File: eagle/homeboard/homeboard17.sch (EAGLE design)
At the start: 127 parts, among them IC1 XCF02S, IC2 25LC080SN, IC3 ATMEGA32U2-TQFP, Q5 BC848SMD, Q6 BC848SMD, Q7 BC848SMD, Q8 BC848SMD, T1 BSS138, T2 BC848, T3 BSS138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

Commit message: cas
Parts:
- removed X1: 1503_04, con-lumberg:1503_04
- added T4: BC848, transistor:BC848
- added X8: STEREOJACK, cpcfpga:STEREOJACK
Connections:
- removed net AASA: SV1.8, U1B5.IO_L31N_5D4
- removed net N$104: SV1.6, U1B5.IO_L28N_5D6
- removed net QQQQ: SV1.7, U1B5.IO_L31P_5D5
- new net AA: SV1.6, U1B5.IO_L28P_5D7
- new net ABAB: SV1.8, U1B5.IO_L31P_5D5
- new net BB: SV1.7, U1B5.IO_L28N_5D6
- net CASIN: now also U1B2.IO_L01P_2VRN_2
- net CSYNC: now also U1B5.IO_L31N_5D4; no longer U1B5.IO_L28P_5D7
- net GND: now also X8.1; no longer X1.2
- net N$61: now also X8.2, X8.3, X8.4, X8.5; no longer X1.1
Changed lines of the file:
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@@
 <part name="C2" library="resistor" deviceset="C-EU" device="C0603" value="100nF"/>
 <part name="T2" library="transistor" deviceset="BC848" device=""/>
-<part name="X1" library="con-lumberg" deviceset="1503_04" device=""/>
 <part name="R22" library="rcl" deviceset="R-EU_" device="R0805" value="1000"/>
 <part name="X3" library="mini_din" deviceset="MINI_DIN_6" device=""/>
@@
 <part name="PWR_HDR" library="jumper" deviceset="JP1Q" device=""/>
 <part name="SUPPLY21" library="supply2" deviceset="GND" device=""/>
+<part name="X8" library="cpcfpga" deviceset="STEREOJACK" device=""/>
+<part name="T4" library="transistor" deviceset="BC848" device=""/>
 </parts>
 <sheets>
@@
 <instance part="C2" gate="G$1" x="492.76" y="-50.8" rot="R90"/>
 <instance part="T2" gate="G$1" x="513.08" y="-50.8"/>
-<instance part="X1" gate="G$1" x="464.82" y="-55.88" rot="R180"/>
 <instance part="R22" gate="G$1" x="508" y="-35.56" rot="R180"/>
 <instance part="X3" gate="G$1" x="279.4" y="-226.06"/>
@@
 <instance part="PWR_HDR" gate="A" x="-297.18" y="50.8" rot="R90"/>
 <instance part="SUPPLY21" gate="GND" x="-289.56" y="38.1"/>
+<instance part="X8" gate="1" x="447.04" y="-58.42" rot="MR0"/>
+<instance part="T4" gate="G$1" x="416.56" y="-33.02"/>
 </instances>
 <busses>
@@
 <wire x1="500.38" y1="-66.04" x2="515.62" y2="-66.04" width="0.1524" layer="91"/>
 <pinref part="R17" gate="G$1" pin="1"/>
-<wire x1="469.9" y1="-66.04" x2="487.68" y2="-66.04" width="0.1524" layer="91"/>
+<wire x1="459.74" y1="-66.04" x2="487.68" y2="-66.04" width="0.1524" layer="91"/>
 <wire x1="487.68" y1="-66.04" x2="500.38" y2="-66.04" width="0.1524" layer="91"/>
 <junction x="487.68" y="-66.04"/>
 <junction x="500.38" y="-66.04"/>
-<pinref part="X1" gate="G$1" pin="2"/>
-<wire x1="469.9" y1="-66.04" x2="469.9" y2="-58.42" width="0.1524" layer="91"/>
 <wire x1="523.24" y1="-66.04" x2="515.62" y2="-66.04" width="0.1524" layer="91"/>
 <junction x="515.62" y="-66.04"/>
 <label x="523.24" y="-66.04" size="1.778" layer="95"/>
+<pinref part="X8" gate="1" pin="1"/>
 </segment>
 <segment>
@@
 </segment>
 <segment>
-<wire x1="99.06" y1="-66.04" x2="139.7" y2="-66.04" width="0.1524" layer="91"/>
-<wire x1="139.7" y1="-66.04" x2="139.7" y2="-40.64" width="0.1524" layer="91"/>
-<pinref part="U1" gate="B5" pin="IO_L28P_5D7"/>
-<label x="99.06" y="-66.04" size="1.778" layer="95"/>
+<pinref part="U1" gate="B5" pin="IO_L31N_5D4"/>
+<wire x1="99.06" y1="-73.66" x2="137.16" y2="-73.66" width="0.1524" layer="91"/>
+<wire x1="137.16" y1="-73.66" x2="137.16" y2="-40.64" width="0.1524" layer="91"/>
+<label x="99.06" y="-73.66" size="1.778" layer="95"/>
 </segment>
 </net>
@@
 <junction x="515.62" y="-55.88"/>
 <label x="523.24" y="-55.88" size="1.778" layer="95"/>
+</segment>
+<segment>
+<pinref part="U1" gate="B2" pin="IO_L01P_2VRN_2"/>
+<wire x1="210.82" y1="55.88" x2="231.14" y2="55.88" width="0.1524" layer="91"/>
+<label x="231.14" y="55.88" size="1.778" layer="95"/>
 </segment>
 </net>
@@
 <wire x1="490.22" y1="-50.8" x2="487.68" y2="-50.8" width="0.1524" layer="91"/>
 <pinref part="R17" gate="G$1" pin="2"/>
-<wire x1="487.68" y1="-50.8" x2="469.9" y2="-50.8" width="0.1524" layer="91"/>
 <wire x1="487.68" y1="-55.88" x2="487.68" y2="-50.8" width="0.1524" layer="91"/>
+<pinref part="X8" gate="1" pin="2"/>
+<wire x1="459.74" y1="-63.5" x2="464.82" y2="-63.5" width="0.1524" layer="91"/>
+<wire x1="464.82" y1="-63.5" x2="477.52" y2="-63.5" width="0.1524" layer="91"/>
+<wire x1="477.52" y1="-63.5" x2="477.52" y2="-55.88" width="0.1524" layer="91"/>
+<wire x1="477.52" y1="-55.88" x2="477.52" y2="-50.8" width="0.1524" layer="91"/>
+<wire x1="477.52" y1="-50.8" x2="487.68" y2="-50.8" width="0.1524" layer="91"/>
 <junction x="487.68" y="-50.8"/>
-<pinref part="X1" gate="G$1" pin="1"/>
+<pinref part="X8" gate="1" pin="5"/>
+<wire x1="459.74" y1="-55.88" x2="464.82" y2="-55.88" width="0.1524" layer="91"/>
+<junction x="477.52" y="-55.88"/>
+<pinref part="X8" gate="1" pin="4"/>
+<wire x1="464.82" y1="-55.88" x2="477.52" y2="-55.88" width="0.1524" layer="91"/>
+<wire x1="459.74" y1="-58.42" x2="464.82" y2="-58.42" width="0.1524" layer="91"/>
+<wire x1="464.82" y1="-58.42" x2="464.82" y2="-55.88" width="0.1524" layer="91"/>
+<junction x="464.82" y="-55.88"/>
+<pinref part="X8" gate="1" pin="3"/>
+<wire x1="459.74" y1="-60.96" x2="464.82" y2="-60.96" width="0.1524" layer="91"/>
+<wire x1="464.82" y1="-60.96" x2="464.82" y2="-63.5" width="0.1524" layer="91"/>
+<junction x="464.82" y="-63.5"/>
 </segment>
 </net>
@@
 </segment>
 </net>
-<net name="N$104" class="0">
-<segment>
-<wire x1="45.72" y1="-93.98" x2="45.72" y2="-66.04" width="0.1524" layer="91"/>
-<wire x1="76.2" y1="-93.98" x2="45.72" y2="-93.98" width="0.1524" layer="91"/>
-<wire x1="76.2" y1="-93.98" x2="76.2" y2="-68.58" width="0.1524" layer="91"/>
+<net name="BB" class="0">
+<segment>
 <pinref part="U1" gate="B5" pin="IO_L28N_5D6"/>
-<wire x1="76.2" y1="-68.58" x2="142.24" y2="-68.58" width="0.1524" layer="91"/>
+<wire x1="78.74" y1="-68.58" x2="142.24" y2="-68.58" width="0.1524" layer="91"/>
 <wire x1="142.24" y1="-68.58" x2="142.24" y2="-40.64" width="0.1524" layer="91"/>
 <label x="99.06" y="-68.58" size="1.778" layer="95"/>
-<pinref part="SV1" gate="1" pin="6"/>
-</segment>
-</net>
-<net name="QQQQ" class="0">
-<segment>
-<pinref part="U1" gate="B5" pin="IO_L31P_5D5"/>
-<wire x1="134.62" y1="-71.12" x2="134.62" y2="-40.64" width="0.1524" layer="91"/>
-<wire x1="134.62" y1="-71.12" x2="78.74" y2="-71.12" width="0.1524" layer="91"/>
-<label x="99.06" y="-71.12" size="1.778" layer="95"/>
-<wire x1="78.74" y1="-96.52" x2="48.26" y2="-96.52" width="0.1524" layer="91"/>
-<wire x1="48.26" y1="-96.52" x2="48.26" y2="-66.04" width="0.1524" layer="91"/>
-<wire x1="78.74" y1="-96.52" x2="78.74" y2="-71.12" width="0.1524" layer="91"/>
 <pinref part="SV1" gate="1" pin="7"/>
-</segment>
-</net>
-<net name="AASA" class="0">
-<segment>
-<pinref part="U1" gate="B5" pin="IO_L31N_5D4"/>
-<wire x1="81.28" y1="-73.66" x2="137.16" y2="-73.66" width="0.1524" layer="91"/>
-<wire x1="137.16" y1="-73.66" x2="137.16" y2="-40.64" width="0.1524" layer="91"/>
-<label x="99.06" y="-73.66" size="1.778" layer="95"/>
-<wire x1="81.28" y1="-99.06" x2="50.8" y2="-99.06" width="0.1524" layer="91"/>
-<wire x1="50.8" y1="-99.06" x2="50.8" y2="-66.04" width="0.1524" layer="91"/>
-<wire x1="81.28" y1="-73.66" x2="81.28" y2="-99.06" width="0.1524" layer="91"/>
-<pinref part="SV1" gate="1" pin="8"/>
+<wire x1="48.26" y1="-66.04" x2="48.26" y2="-96.52" width="0.1524" layer="91"/>
+<wire x1="48.26" y1="-96.52" x2="78.74" y2="-96.52" width="0.1524" layer="91"/>
+<wire x1="78.74" y1="-96.52" x2="78.74" y2="-68.58" width="0.1524" layer="91"/>
 </segment>
 </net>
@@
 </segment>
 </net>
+<net name="AA" class="0">
+<segment>
+<wire x1="76.2" y1="-66.04" x2="139.7" y2="-66.04" width="0.1524" layer="91"/>
+<wire x1="139.7" y1="-66.04" x2="139.7" y2="-40.64" width="0.1524" layer="91"/>
+<pinref part="U1" gate="B5" pin="IO_L28P_5D7"/>
+<label x="99.06" y="-66.04" size="1.778" layer="95"/>
+<wire x1="76.2" y1="-66.04" x2="76.2" y2="-93.98" width="0.1524" layer="91"/>
+<pinref part="SV1" gate="1" pin="6"/>
+<wire x1="76.2" y1="-93.98" x2="45.72" y2="-93.98" width="0.1524" layer="91"/>
+<wire x1="45.72" y1="-93.98" x2="45.72" y2="-66.04" width="0.1524" layer="91"/>
+</segment>
+</net>
+<net name="ABAB" class="0">
+<segment>
+<pinref part="U1" gate="B5" pin="IO_L31P_5D5"/>
+<wire x1="134.62" y1="-71.12" x2="134.62" y2="-40.64" width="0.1524" layer="91"/>
+<wire x1="134.62" y1="-71.12" x2="81.28" y2="-71.12" width="0.1524" layer="91"/>
+<label x="99.06" y="-71.12" size="1.778" layer="95"/>
+<wire x1="81.28" y1="-99.06" x2="50.8" y2="-99.06" width="0.1524" layer="91"/>
+<wire x1="50.8" y1="-99.06" x2="50.8" y2="-66.04" width="0.1524" layer="91"/>
+<pinref part="SV1" gate="1" pin="8"/>
+<wire x1="81.28" y1="-71.12" x2="81.28" y2="-99.06" width="0.1524" layer="91"/>
+</segment>
+</net>

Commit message: mah
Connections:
- new net XX_X: U1B2.IO_L01P_2VRN_2
- net CASIN: now also U1B1.IO_L31N_1VREF_1; no longer U1B2.IO_L01P_2VRN_2
- net CLK16: now also U1B0.IO_L32P_0GCLK6; no longer U1B1.IO_L32N_1GCLK5
- net FPGA_RESET: now also U1B1.IO_L32N_1GCLK5; no longer U1B1.IO_L32P_1GCLK4
- net N$8: no longer U1B0.IO_L32P_0GCLK6
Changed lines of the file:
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@@
 </segment>
 <segment>
-<pinref part="U1" gate="B2" pin="IO_L01P_2VRN_2"/>
-<wire x1="210.82" y1="55.88" x2="231.14" y2="55.88" width="0.1524" layer="91"/>
-<label x="231.14" y="55.88" size="1.778" layer="95"/>
+<pinref part="U1" gate="B1" pin="IO_L31N_1VREF_1"/>
+<wire x1="177.8" y1="73.66" x2="177.8" y2="111.76" width="0.1524" layer="91"/>
+<wire x1="177.8" y1="111.76" x2="154.94" y2="111.76" width="0.1524" layer="91"/>
+<label x="154.94" y="111.76" size="1.778" layer="95"/>
 </segment>
 </net>
@@
 </segment>
 <segment>
-<pinref part="U1" gate="B1" pin="IO_L32N_1GCLK5"/>
-<wire x1="182.88" y1="73.66" x2="182.88" y2="116.84" width="0.1524" layer="91"/>
-<wire x1="182.88" y1="116.84" x2="149.86" y2="116.84" width="0.1524" layer="91"/>
+<wire x1="147.32" y1="116.84" x2="149.86" y2="116.84" width="0.1524" layer="91"/>
 <label x="149.86" y="116.84" size="1.778" layer="95"/>
+<pinref part="U1" gate="B0" pin="IO_L32P_0GCLK6"/>
+<wire x1="147.32" y1="73.66" x2="147.32" y2="116.84" width="0.1524" layer="91"/>
 </segment>
 </net>
@@
 <segment>
 <pinref part="SV3" gate="1" pin="10"/>
-<pinref part="U1" gate="B0" pin="IO_L32P_0GCLK6"/>
-<wire x1="106.68" y1="111.76" x2="147.32" y2="111.76" width="0.1524" layer="91"/>
-<wire x1="147.32" y1="111.76" x2="147.32" y2="73.66" width="0.1524" layer="91"/>
+<wire x1="106.68" y1="111.76" x2="137.16" y2="111.76" width="0.1524" layer="91"/>
 </segment>
 </net>
 <net name="FPGA_RESET" class="0">
 <segment>
-<pinref part="U1" gate="B1" pin="IO_L32P_1GCLK4"/>
-<wire x1="180.34" y1="73.66" x2="180.34" y2="114.3" width="0.1524" layer="91"/>
-<wire x1="180.34" y1="114.3" x2="149.86" y2="114.3" width="0.1524" layer="91"/>
+<wire x1="182.88" y1="114.3" x2="149.86" y2="114.3" width="0.1524" layer="91"/>
 <label x="149.86" y="114.3" size="1.778" layer="95"/>
+<pinref part="U1" gate="B1" pin="IO_L32N_1GCLK5"/>
+<wire x1="182.88" y1="73.66" x2="182.88" y2="114.3" width="0.1524" layer="91"/>
 </segment>
 <segment>
@@
 </segment>
 </net>
+<net name="XX_X" class="0">
+<segment>
+<pinref part="U1" gate="B2" pin="IO_L01P_2VRN_2"/>
+<wire x1="210.82" y1="55.88" x2="231.14" y2="55.88" width="0.1524" layer="91"/>
+<label x="231.14" y="55.88" size="1.778" layer="95"/>
+</segment>
+</net>

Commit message: mah
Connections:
- net N$8: now also U1B1.IO_L32P_1GCLK4
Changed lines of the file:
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@@
 <segment>
 <pinref part="U1" gate="B1" pin="IO_L31N_1VREF_1"/>
-<wire x1="177.8" y1="73.66" x2="177.8" y2="111.76" width="0.1524" layer="91"/>
-<wire x1="177.8" y1="111.76" x2="154.94" y2="111.76" width="0.1524" layer="91"/>
-<label x="154.94" y="111.76" size="1.778" layer="95"/>
+<wire x1="177.8" y1="73.66" x2="177.8" y2="114.3" width="0.1524" layer="91"/>
+<wire x1="177.8" y1="114.3" x2="154.94" y2="114.3" width="0.1524" layer="91"/>
+<label x="154.94" y="114.3" size="1.778" layer="95"/>
 </segment>
 </net>
@@
 </segment>
 <segment>
-<wire x1="147.32" y1="116.84" x2="149.86" y2="116.84" width="0.1524" layer="91"/>
-<label x="149.86" y="116.84" size="1.778" layer="95"/>
+<wire x1="147.32" y1="119.38" x2="149.86" y2="119.38" width="0.1524" layer="91"/>
+<label x="149.86" y="119.38" size="1.778" layer="95"/>
 <pinref part="U1" gate="B0" pin="IO_L32P_0GCLK6"/>
-<wire x1="147.32" y1="73.66" x2="147.32" y2="116.84" width="0.1524" layer="91"/>
+<wire x1="147.32" y1="73.66" x2="147.32" y2="119.38" width="0.1524" layer="91"/>
 </segment>
 </net>
@@
 <segment>
 <pinref part="SV3" gate="1" pin="10"/>
-<wire x1="106.68" y1="111.76" x2="137.16" y2="111.76" width="0.1524" layer="91"/>
+<pinref part="U1" gate="B1" pin="IO_L32P_1GCLK4"/>
+<wire x1="106.68" y1="111.76" x2="180.34" y2="111.76" width="0.1524" layer="91"/>
+<wire x1="180.34" y1="111.76" x2="180.34" y2="73.66" width="0.1524" layer="91"/>
 </segment>
 </net>
 <net name="FPGA_RESET" class="0">
 <segment>
-<wire x1="182.88" y1="114.3" x2="149.86" y2="114.3" width="0.1524" layer="91"/>
-<label x="149.86" y="114.3" size="1.778" layer="95"/>
+<wire x1="182.88" y1="116.84" x2="149.86" y2="116.84" width="0.1524" layer="91"/>
+<label x="149.86" y="116.84" size="1.778" layer="95"/>
 <pinref part="U1" gate="B1" pin="IO_L32N_1GCLK5"/>
-<wire x1="182.88" y1="73.66" x2="182.88" y2="114.3" width="0.1524" layer="91"/>
-</segment>
-<segment>
+<wire x1="182.88" y1="73.66" x2="182.88" y2="116.84" width="0.1524" layer="91"/>
+</segment>
+<segment>

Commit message: updated drill hole in scart socket
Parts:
- removed X2: SCART-F, con-hirschmann:SCART-F
- added X1: SCART-CLIP, cpcfpga:SCART-CLIP
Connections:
- net N$30 renamed JOY1_FIRE1
- net N$31 renamed JOY1_FIRE2
- net N$32 renamed JOY1_RIGHT
- net N$33 renamed JOY1_LEFT
- net N$34 renamed JOY1_DOWN
- net N$37 renamed JOY1_UP
- removed net N$41: R40.2, X4-1.F
- removed net N$44: R41.2, X4-2.F
- removed net N$45: R42.2, X4-3.F
- removed net N$46: R43.2, X4-4.F
- removed net N$47: R44.2, X4-6.F
- removed net N$48: R45.2, X4-7.F
- new net JOY0_DOWN: R41.2, U1B1.IO_L28P_1, X4-2.F
- new net JOY0_FIRE1: R45.2, U1B1.IO, X4-7.F
- new net JOY0_FIRE2: R44.2, U1B1.IO_L28N_1, X4-6.F
- new net JOY0_LEFT: R42.2, U1B1.IO_L01N_1VRP_1, X4-3.F
- new net JOY0_RIGHT: R43.2, U1B1.IO_L01P_1VRN_1, X4-4.F
- new net JOY0_UP: R40.2, U1B1.IO_L31P_1, X4-1.F
- net AINLEFT: now also X1.6; no longer X2.6
- net AINRIGHT: now also X1.2; no longer X2.2
- net COMPIN: now also X1.20; no longer X2.20
- net GND: now also X1.13, X1.14, X1.17, X1.18, X1.21, X1.4, X1.5, X1.9; no longer X2.13, X2.14, X2.17, X2.18, X2.21, X2.4, X2.5, X2.9
- net SCART_BLANKING: now also X1.16; no longer X2.16
- net SCART_BLUE: now also X1.7; no longer X2.7
- net SCART_COMP: now also X1.19; no longer X2.19
- net SCART_GREEN: now also X1.11; no longer X2.11
- net SCART_LEFT: now also X1.3; no longer X2.3
- net SCART_MODE: now also X1.8; no longer X2.8
- net SCART_RED: now also X1.15; no longer X2.15
- net SCART_RIGHT: now also X1.1; no longer X2.1
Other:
- moved on the sheet: C1, C3, C4, C5, Q5, Q6, Q7, Q8, R10, R11, R12, R13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

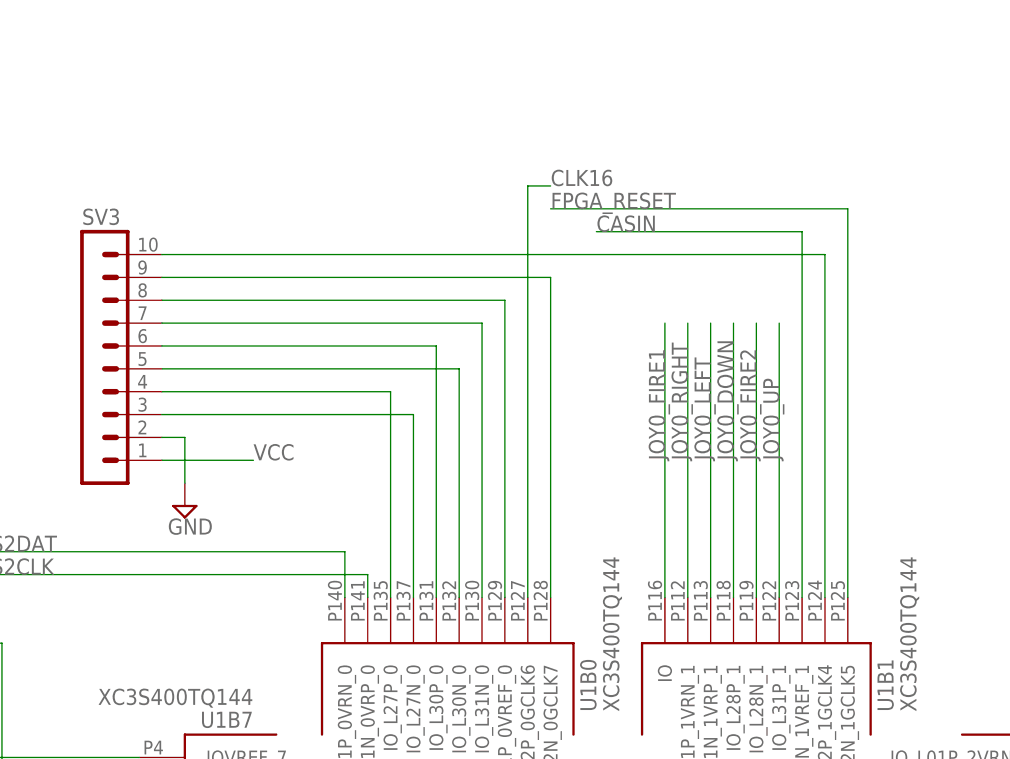
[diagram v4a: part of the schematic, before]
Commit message: re-ordering pins
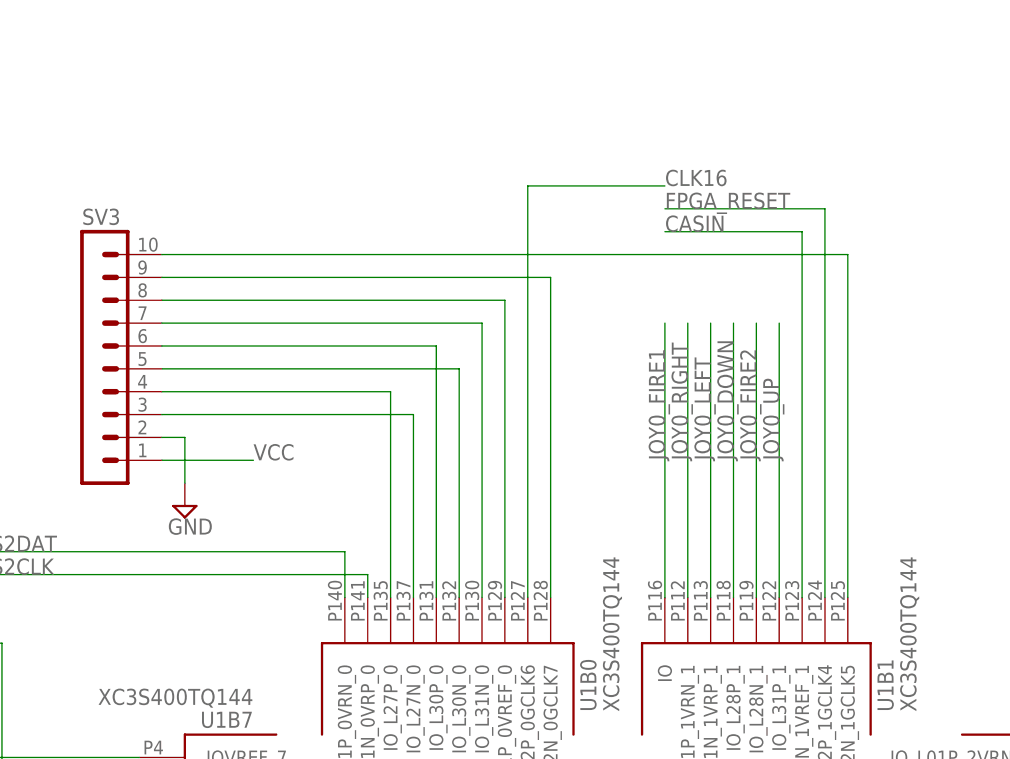
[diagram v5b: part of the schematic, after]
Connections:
- net FPGA_RESET: now also U1B1.IO_L32P_1GCLK4; no longer U1B1.IO_L32N_1GCLK5
- net N$8: now also U1B1.IO_L32N_1GCLK5; no longer U1B1.IO_L32P_1GCLK4
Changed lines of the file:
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@@
 <pinref part="U1" gate="B1" pin="IO_L31N_1VREF_1"/>
 <wire x1="177.8" y1="73.66" x2="177.8" y2="114.3" width="0.1524" layer="91"/>
-<wire x1="177.8" y1="114.3" x2="154.94" y2="114.3" width="0.1524" layer="91"/>
-<label x="154.94" y="114.3" size="1.778" layer="95"/>
+<wire x1="177.8" y1="114.3" x2="162.56" y2="114.3" width="0.1524" layer="91"/>
+<label x="162.56" y="114.3" size="1.778" layer="95"/>
 </segment>
 </net>
@@
 </segment>
 <segment>
-<wire x1="147.32" y1="119.38" x2="149.86" y2="119.38" width="0.1524" layer="91"/>
-<label x="149.86" y="119.38" size="1.778" layer="95"/>
+<wire x1="147.32" y1="119.38" x2="162.56" y2="119.38" width="0.1524" layer="91"/>
+<label x="162.56" y="119.38" size="1.778" layer="95"/>
 <pinref part="U1" gate="B0" pin="IO_L32P_0GCLK6"/>
 <wire x1="147.32" y1="73.66" x2="147.32" y2="119.38" width="0.1524" layer="91"/>
@@
 <segment>
 <pinref part="SV3" gate="1" pin="10"/>
+<wire x1="106.68" y1="111.76" x2="182.88" y2="111.76" width="0.1524" layer="91"/>
+<pinref part="U1" gate="B1" pin="IO_L32N_1GCLK5"/>
+<wire x1="182.88" y1="111.76" x2="182.88" y2="73.66" width="0.1524" layer="91"/>
+</segment>
+</net>
+<net name="FPGA_RESET" class="0">
+<segment>
+<wire x1="180.34" y1="116.84" x2="162.56" y2="116.84" width="0.1524" layer="91"/>
+<label x="162.56" y="116.84" size="1.778" layer="95"/>
 <pinref part="U1" gate="B1" pin="IO_L32P_1GCLK4"/>
-<wire x1="106.68" y1="111.76" x2="180.34" y2="111.76" width="0.1524" layer="91"/>
-<wire x1="180.34" y1="111.76" x2="180.34" y2="73.66" width="0.1524" layer="91"/>
-</segment>
-</net>
-<net name="FPGA_RESET" class="0">
-<segment>
-<wire x1="182.88" y1="116.84" x2="149.86" y2="116.84" width="0.1524" layer="91"/>
-<label x="149.86" y="116.84" size="1.778" layer="95"/>
-<pinref part="U1" gate="B1" pin="IO_L32N_1GCLK5"/>
-<wire x1="182.88" y1="73.66" x2="182.88" y2="116.84" width="0.1524" layer="91"/>
-</segment>
-<segment>
+<wire x1="180.34" y1="116.84" x2="180.34" y2="73.66" width="0.1524" layer="91"/>
+</segment>
+<segment>

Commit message: mah
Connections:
- removed net XX_X: U1B2.IO_L01P_2VRN_2
- net FL_DI: now also U1B2.IO_L20N_2
- net FL_DO: now also U1B2.IO_L21N_2
- net FL_HOLD: now also U1B2.IO_L01N_2VRP_2
- net FL_SCLK: now also U1B2.IO_L01P_2VRN_2
- net FL_SEL: now also U1B2.IO_L21P_2
- net FL_WP: now also U1B2.IO_L20P_2
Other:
- moved on the sheet: C37, C38, C39, C40, IC2, IC3, Q1, R53, R54, SJ1, SJ2, X6
